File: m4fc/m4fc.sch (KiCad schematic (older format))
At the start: 39 parts

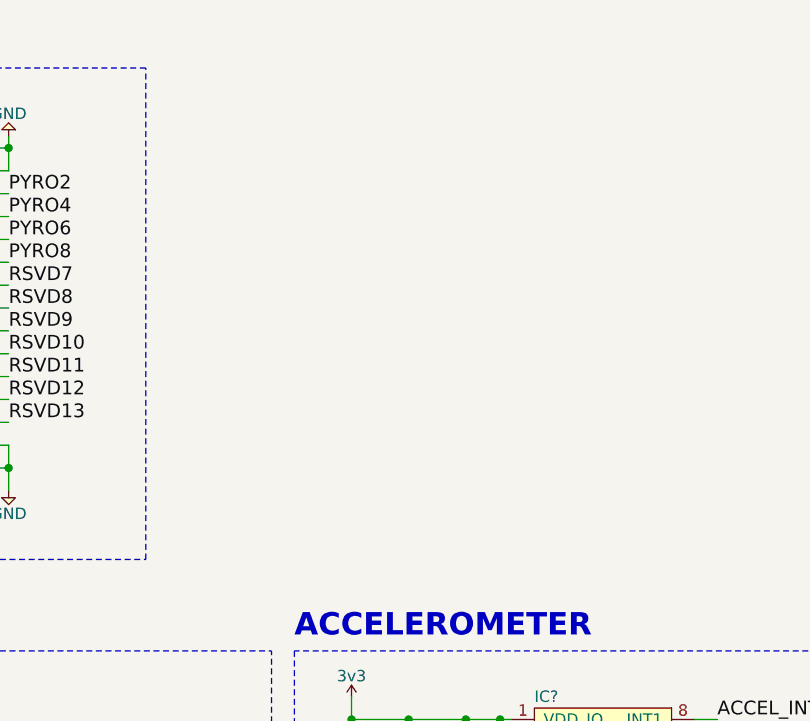
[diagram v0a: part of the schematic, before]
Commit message: Add camera interconnect
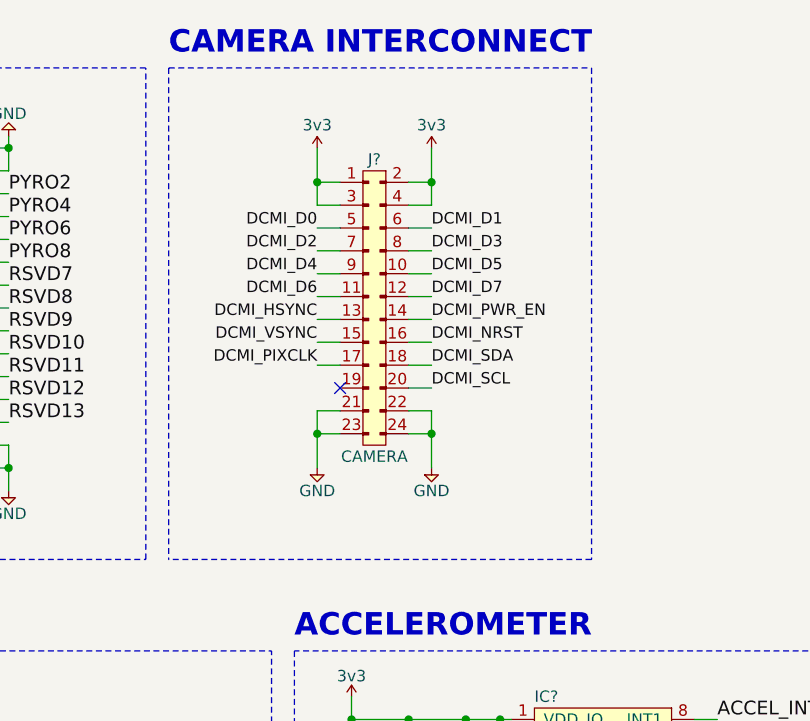
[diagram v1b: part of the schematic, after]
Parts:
- added J?: CAMERA, symbol cusf-kicad:CONN_02x12
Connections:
- net 3v3: now also J?.1, J?.2, J?.3, J?.4
- net GND: now also J?.21, J?.22, J?.23, J?.24
- new net DCMI_D0: J?.5
- new net DCMI_D1: J?.6
- new net DCMI_D2: J?.7
- new net DCMI_D3: J?.8
- new net DCMI_D4: J?.9
- new net DCMI_D5: J?.10
- new net DCMI_D6: J?.11
- new net DCMI_D7: J?.12
- new net DCMI_HSYNC: J?.13
- new net DCMI_NRST: J?.16
- new net DCMI_PIXCLK: J?.17
- new net DCMI_PWR_EN: J?.14
- new net DCMI_SCL: J?.20
- new net DCMI_SDA: J?.18
- new net DCMI_VSYNC: J?.15
- no-connect marks 25 -> 26
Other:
- note added: "CAMERA INTERCONNECT"
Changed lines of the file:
@@
 Text Notes 4450 6650 0    98   ~ 20
 BEEPER
+$Comp
+L cusf-kicad:CONN_02x12 J?
+U 1 1 5ED17754
+P 4850 1250
+F 0 "J?" H 4800 1350 50  0000 C CNN
+F 1 "CAMERA" H 4800 50  50  0000 C CNN
+F 2 "" H 4850 1250 50  0001 C CNN
+F 3 "" H 4850 1250 50  0001 C CNN
+	1    4850 1250
+	1    0    0    -1
+$EndComp
+Wire Wire Line
+	4650 1350 4550 1350
+Wire Wire Line
+	4550 1350 4550 1250
+Wire Wire Line
+	4550 1250 4650 1250
+Wire Wire Line
+	4950 1250 5050 1250
+Wire Wire Line
+	5050 1250 5050 1350
+Wire Wire Line
+	4950 1350 5050 1350
+Wire Wire Line
+	5050 1250 5050 1100
+Connection ~ 5050 1250
+Wire Wire Line
+	4550 1100 4550 1250
+Connection ~ 4550 1250
+$Comp
+L cusf-kicad:3v3 #PWR?
+U 1 1 5ED8339B
+P 4550 1100
+F 0 "#PWR?" H 4550 1210 50  0001 L CNN
+F 1 "3v3" H 4550 1200 50  0000 C CNN
+F 2 "" H 4550 1100 50  0001 C CNN
+F 3 "" H 4550 1100 50  0001 C CNN
+	1    4550 1100
+	1    0    0    -1
+$EndComp
+$Comp
+L cusf-kicad:3v3 #PWR?
+U 1 1 5ED836CE
+P 5050 1100
+F 0 "#PWR?" H 5050 1210 50  0001 L CNN
+F 1 "3v3" H 5050 1200 50  0000 C CNN
+F 2 "" H 5050 1100 50  0001 C CNN
+F 3 "" H 5050 1100 50  0001 C CNN
+	1    5050 1100
+	1    0    0    -1
+$EndComp
+Wire Wire Line
+	4650 2350 4550 2350
+Wire Wire Line
+	4550 2350 4550 2500
+Wire Wire Line
+	4550 2350 4550 2250
+Wire Wire Line
+	4550 2250 4650 2250
+Connection ~ 4550 2350
+Wire Wire Line
+	4950 2350 5050 2350
+Wire Wire Line
+	5050 2350 5050 2500
+Wire Wire Line
+	5050 2350 5050 2250
+Wire Wire Line
+	5050 2250 4950 2250
+Connection ~ 5050 2350
+$Comp
+L cusf-kicad:GND #PWR?
+U 1 1 5EDD9C20
+P 4550 2500
+F 0 "#PWR?" H 4420 2540 50  0001 L CNN
+F 1 "GND" H 4550 2400 50  0000 C CNN
+F 2 "" H 4550 2500 50  0001 C CNN
+F 3 "" H 4550 2500 50  0001 C CNN
+	1    4550 2500
+	1    0    0    -1
+$EndComp
+$Comp
+L cusf-kicad:GND #PWR?
+U 1 1 5EDDA6DE
+P 5050 2500
+F 0 "#PWR?" H 4920 2540 50  0001 L CNN
+F 1 "GND" H 5050 2400 50  0000 C CNN
+F 2 "" H 5050 2500 50  0001 C CNN
+F 3 "" H 5050 2500 50  0001 C CNN
+	1    5050 2500
+	1    0    0    -1
+$EndComp
+Wire Wire Line
+	4650 1450 4550 1450
+Wire Wire Line
+	4650 1550 4550 1550
+Wire Wire Line
+	4650 1650 4550 1650
+Wire Wire Line
+	4650 1750 4550 1750
+Wire Wire Line
+	4650 1850 4550 1850
+Wire Wire Line
+	4950 1450 5050 1450
+Wire Wire Line
+	4950 1550 5050 1550
+Wire Wire Line
+	4950 1650 5050 1650
+Wire Wire Line
+	4950 1750 5050 1750
+Wire Wire Line
+	4950 1850 5050 1850
+Wire Wire Line
+	5050 1950 4950 1950
+Wire Wire Line
+	5050 2050 4950 2050
+Wire Wire Line
+	4550 2050 4650 2050
+Wire Wire Line
+	4550 1950 4650 1950
+Text Label 5050 1450 0    50   ~ 0
+DCMI_D1
+Text Label 5050 1550 0    50   ~ 0
+DCMI_D3
+Text Label 5050 1650 0    50   ~ 0
+DCMI_D5
+Text Label 5050 1750 0    50   ~ 0
+DCMI_D7
+Text Label 4550 1750 2    50   ~ 0
+DCMI_D6
+Text Label 4550 1650 2    50   ~ 0
+DCMI_D4
+Text Label 4550 1550 2    50   ~ 0
+DCMI_D2
+Text Label 4550 1450 2    50   ~ 0
+DCMI_D0
+Text Label 4550 2050 2    50   ~ 0
+DCMI_PIXCLK
+Text Label 4550 1950 2    50   ~ 0
+DCMI_VSYNC
+Text Label 4550 1850 2    50   ~ 0
+DCMI_HSYNC
+Text Label 5050 1850 0    50   ~ 0
+DCMI_PWR_EN
+Text Label 5050 1950 0    50   ~ 0
+DCMI_NRST
+Wire Notes Line
+	3900 750  5750 750
+Wire Notes Line
+	5750 750  5750 2900
+Wire Notes Line
+	5750 2900 3900 2900
+Wire Notes Line
+	3900 750  3900 2900
+Text Notes 3900 700  0    98   ~ 20
+CAMERA INTERCONNECT
+Wire Wire Line
+	4950 2150 5050 2150
+Text Label 5050 2050 0    50   ~ 0
+DCMI_SDA
+Text Label 5050 2150 0    50   ~ 0
+DCMI_SCL
+NoConn ~ 4650 2150
 $EndSCHEMATC
